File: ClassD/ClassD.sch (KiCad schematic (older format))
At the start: 28 parts, among them SW1 SW_PUSH, U1 TPA2008D2

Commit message: Updated the schematic with some part numbers and parametrics
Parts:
- removed SW1: SW_PUSH, symbol SW_PUSH
- added P? (x2): BNC, symbol BNC
- added SW?: SPST, symbol SPST
- C1, C10, C3, C4: ConradPN (none) -> Value; Fieldname (none) -> Value; Voltage (none) -> 10 V
- C2: ConradPN (none) -> Value; DigiKeyPN Value -> 1276-2865-1-ND; Fieldname (none) -> Value; Voltage (none) -> 16 V
- C5: value 120 pF -> 220 pF; ConradPN (none) -> Value; DigiKeyPN Value -> 1276-1059-1-ND; Fieldname (none) -> Value; Voltage (none) -> 50 V
- C6, C7, C8, C9: ConradPN (none) -> Value; Fieldname (none) -> Value; Voltage (none) -> 16 V
- C? (x2): value 4.7 μF -> 470 nF; ConradPN (none) -> Value; Fieldname (none) -> Value; Voltage (none) -> 50 V
- C? (x4): ConradPN (none) -> Value; Fieldname (none) -> Value; Voltage (none) -> 50 V
- RV1: ConradPN (none) -> Value; DigiKeyPN (none) -> 3362P-503TLF-ND; Fieldname (none) -> Value; Voltage (none) -> Value
- U1: ConradPN (none) -> Value; DigiKeyPN (none) -> 296-17158-1-ND; Fieldname (none) -> Value; Voltage (none) -> Value

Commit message: Updated the BOM specifications and added a regulator for VDD
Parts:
- added C12, C13: 1 μF, symbol C
- added P1: CONN_01X02, symbol CONN_01X02
- added U2: MCP1703T-5002E, symbol MCP1703T-5002E
- L1, L2, L3, L4: renamed from L?; ConradPN (none) -> Value; DigiKeyPN (none) -> 587-2618-1-ND; Fieldname (none) -> Value; Voltage (none) -> Value
- P2: renamed from P?; ConradPN (none) -> Value; DigiKeyPN (none) -> CP-1401-ND; Fieldname (none) -> Value; Voltage (none) -> Value
- P3: renamed from P?; ConradPN (none) -> Value; DigiKeyPN (none) -> CP-1402-ND; Fieldname (none) -> Value; Voltage (none) -> Value
- SP1: renamed from SP?; ConradPN (none) -> Value; DigiKeyPN (none) -> CP-1401-ND; Fieldname (none) -> Value; Voltage (none) -> Value
- SP2: renamed from SP?; ConradPN (none) -> Value; DigiKeyPN (none) -> CP-1402-ND; Fieldname (none) -> Value; Voltage (none) -> Value
- SW1: renamed from SW?; DigiKeyPN P8086SCT-ND -> FSM2JSMAA-SI-ND
- gave numbers to parts that had none: 6
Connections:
- net labels added: VIN
- wire segments 87 -> 97
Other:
- moved on the sheet: C1, C10, C11, C14, C15, C16, C17, C18, C19, C2, C3, C4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

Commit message: Updated the digikey part numbers etc.
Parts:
- removed C2: 10 μF, symbol C
- added C2: 10 μF, symbol CP
- L1, L2, L3, L4: DigiKeyPN 587-2618-1-ND -> 490-8418-1-ND
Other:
- note added: "For higher frequency transients, spikes, or digital hash on the line, \na good low equivalent-series-resistance (ESR) ceramic capacitor, \ntypically 0.1 μF, placed as close as possible to the device V DD \nterminal works best. For filtering lower-frequency noise signals, \na larger aluminum electrolytic capacitor of 10 μF or greater \nplaced near the audio power amplifier is recommended."
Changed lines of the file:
@@
 VDD
 $Comp
-L GND #PWR01
+L GND #PWR4
 U 1 1 56B5F2B5
 P 5850 5650
-F 0 "#PWR01" H 5850 5400 50  0001 C CNN
+F 0 "#PWR4" H 5850 5400 50  0001 C CNN
 F 1 "GND" H 5850 5500 50  0000 C CNN
 F 2 "" H 5850 5650 50  0000 C CNN
@@
 $EndComp
 $Comp
-L C C2
-U 1 1 56B60670
-P 2950 2700
-F 0 "C2" H 3000 2800 50  0000 L CNN
-F 1 "10 μF" H 2700 2600 50  0000 L CNN
-F 2 "" H 2988 2550 50  0000 C CNN
-F 3 "" H 2950 2700 50  0000 C CNN
-F 4 " 1276-2865-1-ND " H 2950 2700 60  0001 C CNN "DigiKeyPN"
-F 5 "16 V" H 2800 2500 60  0000 C CNN "Voltage"
-F 6 "Value" H 2950 2700 60  0001 C CNN "ConradPN"
-F 7 "Value" H 2950 2700 60  0001 C CNN "Fieldname"
-	1    2950 2700
-	1    0    0    -1
-$EndComp
-$Comp
-L GND #PWR02
+L GND #PWR3
 U 1 1 56B607D9
 P 2650 3200
-F 0 "#PWR02" H 2650 2950 50  0001 C CNN
+F 0 "#PWR3" H 2650 2950 50  0001 C CNN
 F 1 "GND" H 2650 3050 50  0000 C CNN
 F 2 "" H 2650 3200 50  0000 C CNN
@@
 $EndComp
 $Comp
-L GND #PWR03
+L GND #PWR5
 U 1 1 56B60A69
 P 6350 5550
-F 0 "#PWR03" H 6350 5300 50  0001 C CNN
+F 0 "#PWR5" H 6350 5300 50  0001 C CNN
 F 1 "GND" H 6350 5400 50  0000 C CNN
 F 2 "" H 6350 5550 50  0000 C CNN
@@
 ~SHUTDOWN
 $Comp
-L GND #PWR04
+L GND #PWR1
 U 1 1 56B6395C
 P 2000 6000
-F 0 "#PWR04" H 2000 5750 50  0001 C CNN
+F 0 "#PWR1" H 2000 5750 50  0001 C CNN
 F 1 "GND" H 2000 5850 50  0000 C CNN
 F 2 "" H 2000 6000 50  0000 C CNN
@@
 F 2 "" H 7000 1900 50  0000 C CNN
 F 3 "" H 7000 1900 50  0000 C CNN
-F 4 "587-2618-1-ND" H 7000 1900 60  0001 C CNN "DigiKeyPN"
+F 4 "490-8418-1-ND" H 7000 1900 60  0001 C CNN "DigiKeyPN"
 F 5 "Value" H 7000 1900 60  0001 C CNN "Voltage"
 F 6 "Value" H 7000 1900 60  0001 C CNN "ConradPN"
@@
 F 2 "" H 7000 2550 50  0000 C CNN
 F 3 "" H 7000 2550 50  0000 C CNN
-F 4 "587-2618-1-ND" H 7000 2550 60  0001 C CNN "DigiKeyPN"
+F 4 "490-8418-1-ND" H 7000 2550 60  0001 C CNN "DigiKeyPN"
 F 5 "Value" H 7000 2550 60  0001 C CNN "Voltage"
 F 6 "Value" H 7000 2550 60  0001 C CNN "ConradPN"
@@
 F 2 "" H 7150 3350 50  0000 C CNN
 F 3 "" H 7150 3350 50  0000 C CNN
-F 4 "587-2618-1-ND" H 7150 3350 60  0001 C CNN "DigiKeyPN"
+F 4 "490-8418-1-ND" H 7150 3350 60  0001 C CNN "DigiKeyPN"
 F 5 "Value" H 7150 3350 60  0001 C CNN "Voltage"
 F 6 "Value" H 7150 3350 60  0001 C CNN "ConradPN"
@@
 F 2 "" H 7150 4050 50  0000 C CNN
 F 3 "" H 7150 4050 50  0000 C CNN
-F 4 "587-2618-1-ND" H 7150 4050 60  0001 C CNN "DigiKeyPN"
+F 4 "490-8418-1-ND" H 7150 4050 60  0001 C CNN "DigiKeyPN"
 F 5 "Value" H 7150 4050 60  0001 C CNN "Voltage"
 F 6 "Value" H 7150 4050 60  0001 C CNN "ConradPN"
@@
 $EndComp
 $Comp
-L GND #PWR05
+L GND #PWR6
 U 1 1 56B66F4B
 P 7800 2300
-F 0 "#PWR05" H 7800 2050 50  0001 C CNN
+F 0 "#PWR6" H 7800 2050 50  0001 C CNN
 F 1 "GND" H 7800 2150 50  0000 C CNN
 F 2 "" H 7800 2300 50  0000 C CNN
@@
 $EndComp
 $Comp
-L GND #PWR06
+L GND #PWR8
 U 1 1 56B6779F
 P 8150 3800
-F 0 "#PWR06" H 8150 3550 50  0001 C CNN
+F 0 "#PWR8" H 8150 3550 50  0001 C CNN
 F 1 "GND" H 8150 3650 50  0000 C CNN
 F 2 "" H 8150 3800 50  0000 C CNN
@@
 $EndComp
 $Comp
-L GND #PWR07
+L GND #PWR9
 U 1 1 56B68F55
 P 8150 4550
-F 0 "#PWR07" H 8150 4300 50  0001 C CNN
+F 0 "#PWR9" H 8150 4300 50  0001 C CNN
 F 1 "GND" H 8150 4400 50  0000 C CNN
 F 2 "" H 8150 4550 50  0000 C CNN
@@
 $EndComp
 $Comp
-L GND #PWR08
+L GND #PWR7
 U 1 1 56B692A2
 P 7800 3000
-F 0 "#PWR08" H 7800 2750 50  0001 C CNN
+F 0 "#PWR7" H 7800 2750 50  0001 C CNN
 F 1 "GND" H 7800 2850 50  0000 C CNN
 F 2 "" H 7800 3000 50  0000 C CNN
@@
 	2450 1250 2450 1750
 $Comp
-L GND #PWR09
+L GND #PWR2
 U 1 1 56B7932F
 P 2450 1750
-F 0 "#PWR09" H 2450 1500 50  0001 C CNN
+F 0 "#PWR2" H 2450 1500 50  0001 C CNN
 F 1 "GND" H 2450 1600 50  0000 C CNN
 F 2 "" H 2450 1750 50  0000 C CNN
@@
 	7400 2250 7400 2550
 Connection ~ 7400 2550
+Text Notes 7900 5600 0    60   ~ 0
+For higher frequency transients, spikes, or digital hash on the line, \na good low equivalent-series-resistance (ESR) ceramic capacitor, \ntypically 0.1 μF, placed as close as possible to the device V DD \nterminal works best. For filtering lower-frequency noise signals, \na larger aluminum electrolytic capacitor of 10 μF or greater \nplaced near the audio power amplifier is recommended.
+$Comp
+L CP C2
+U 1 1 56B8FB66
+P 2950 2700
+F 0 "C2" H 2975 2800 50  0000 L CNN
+F 1 "10 μF" H 2700 2600 50  0000 L CNN
+F 2 "" H 2988 2550 50  0000 C CNN
+F 3 "" H 2950 2700 50  0000 C CNN
+F 4 "493-2181-1-ND" H 2950 2700 60  0001 C CNN "DigiKeyPN"
+F 5 "16 V" H 2800 2500 60  0000 C CNN "Voltage"
+F 6 "Value" H 2950 2700 60  0001 C CNN "ConradPN"
+F 7 "Value" H 2950 2700 60  0001 C CNN "Fieldname"
+	1    2950 2700
+	1    0    0    -1
+$EndComp
 $EndSCHEMATC

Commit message: Updated the speaker with the link to digi-key
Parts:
- SP1, SP2: Fieldname Value -> (none); Link (none) -> http://www.digikey.de/product-detail/de/AS07108PO-R/668-137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
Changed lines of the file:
@@
 F 5 "Value" H 9100 3700 60  0001 C CNN "Voltage"
 F 6 "Value" H 9100 3700 60  0001 C CNN "ConradPN"
-F 7 "Value" H 9100 3700 60  0001 C CNN "Fieldname"
+F 7 "http://www.digikey.de/product-detail/de/AS07108PO-R/668-1371-ND/1745572" H 9100 3700 60  0001 C CNN "Link"
 	1    9100 3700
 	1    0    0    -1
@@
 F 5 "Value" H 9100 2200 60  0001 C CNN "Voltage"
 F 6 "Value" H 9100 2200 60  0001 C CNN "ConradPN"
-F 7 "Value" H 9100 2200 60  0001 C CNN "Fieldname"
+F 7 "http://www.digikey.de/product-detail/de/AS07108PO-R/668-1371-ND/1745572" H 9100 2200 60  0001 C CNN "Link"
 	1    9100 2200
 	1    0    0    -1

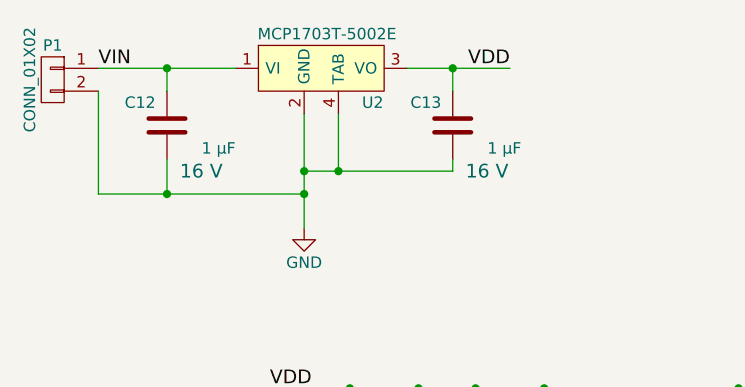
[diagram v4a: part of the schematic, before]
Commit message: Changed the voltage regulator to 1A (for the 4Ohm case)
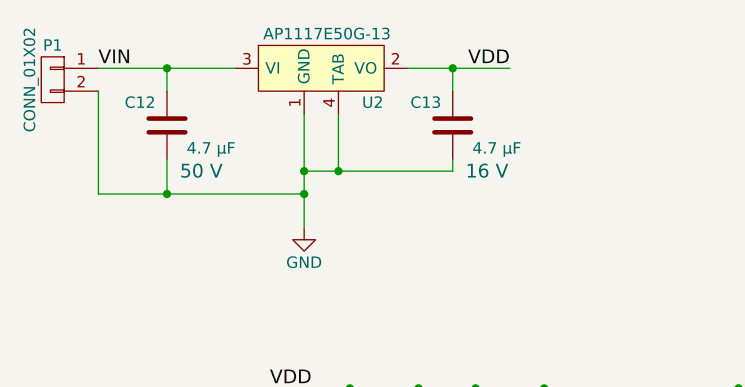
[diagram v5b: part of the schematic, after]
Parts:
- removed U2: MCP1703T-5002E, symbol MCP1703T-5002E
- added U2: AP1117E50G-13, symbol AP1117E50G-13
- C12: value 1 μF -> 4.7 μF; Voltage 16 V -> 50 V
- C13: value 1 μF -> 4.7 μF
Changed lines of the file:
@@
 Wire Wire Line
 	8700 3800 8800 3800
-$Comp
-L MCP1703T-5002E U2
-U 1 1 56B7910E
-P 2450 1050
-F 0 "U2" H 2750 900 50  0000 C CNN
-F 1 "MCP1703T-5002E" H 2550 1200 50  0000 C CNN
-F 2 "" H 2450 1050 50  0000 C CNN
-F 3 "" H 2450 1050 50  0000 C CNN
-F 4 "MCP1703T-5002E/DBCT-ND" H 2450 1050 60  0001 C CNN "DigiKeyPN"
-F 5 "Value" H 2450 1050 60  0001 C CNN "Voltage"
-F 6 "Value" H 2450 1050 60  0001 C CNN "ConradPN"
-F 7 "Value" H 2450 1050 60  0001 C CNN "Fieldname"
-	1    2450 1050
-	1    0    0    -1
-$EndComp
 Wire Wire Line
 	2600 1250 2600 1500
@@
 P 1850 1300
 F 0 "C12" H 1900 1200 50  0000 L CNN
-F 1 "1 μF" H 1550 1400 50  0000 L CNN
+F 1 "4.7 μF" H 1550 1400 50  0000 L CNN
 F 2 "" H 1888 1150 50  0000 C CNN
 F 3 "" H 1850 1300 50  0000 C CNN
 F 4 "Value" H 1850 1300 60  0001 C CNN "DigiKeyPN"
-F 5 "16 V" H 1700 1500 60  0000 C CNN "Voltage"
+F 5 "50 V" H 1700 1500 60  0000 C CNN "Voltage"
 F 6 "Value" H 1850 1300 60  0001 C CNN "ConradPN"
 F 7 "Value" H 1850 1300 60  0001 C CNN "Fieldname"
@@
 P 3100 1300
 F 0 "C13" H 3150 1200 50  0000 L CNN
-F 1 "1 μF" H 2800 1400 50  0000 L CNN
+F 1 "4.7 μF" H 2800 1400 50  0000 L CNN
 F 2 "" H 3138 1150 50  0000 C CNN
 F 3 "" H 3100 1300 50  0000 C CNN
@@
 	1    0    0    -1
 $EndComp
+$Comp
+L AP1117E50G-13 U2
+U 1 1 56BA2D73
+P 2450 1050
+F 0 "U2" H 2750 900 50  0000 C CNN
+F 1 "AP1117E50G-13" H 2550 1200 50  0000 C CNN
+F 2 "" H 2450 1050 50  0000 C CNN
+F 3 "" H 2450 1050 50  0000 C CNN
+F 4 "AP1117E50GDICT-ND" H 2450 1050 60  0001 C CNN "DigiKeyPN"
+F 5 "Value" H 2450 1050 60  0001 C CNN "Voltage"
+F 6 "Value" H 2450 1050 60  0001 C CNN "ConradPN"
+F 7 "http://www.digikey.de/product-detail/de/AP1117E50G-13/AP1117E50GDICT-ND/1301523" H 2450 1050 60  0001 C CNN "Link"
+	1    2450 1050
+	1    0    0    -1
+$EndComp

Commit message: Updated speaker specs
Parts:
- added R1: NOPOP, symbol R
- SP1: DigiKeyPN CP-1401-ND -> GF0771-ND; Link http://www.digikey.de/product-detail/de/AS07108PO-R/668-137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 -> http://www.digikey.de/product-detail/de/GF0771/GF0771-ND/30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
- SP2: DigiKeyPN CP-1402-ND -> GF0771-ND; Link http://www.digikey.de/product-detail/de/AS07108PO-R/668-137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 -> http://www.digikey.de/product-detail/de/GF0771/GF0771-ND/30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
- renumbered C12 to C1, C15 to C10, C18 to C11, C8 to C12, C6 to C13, C9 to C14, C7 to C15, C19 to C16, C5 to C17, C10 to C18, C11 to C19, C13 to C2, C14 to C3, C16 to C4, C1 to C5, C2 to C6, C3 to C7, C4 to C8, C17 to C9, R1 to R3, U2 to U1, U1 to U2
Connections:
- net labels removed: SHUTDOWN
- wire segments 97 -> 101
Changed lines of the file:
@@
 $EndDescr
 $Comp
-L C C8
+L C C12
 U 1 1 56B5D94C
 P 4700 3650
-F 0 "C8" V 4750 3700 50  0000 L CNN
+F 0 "C12" V 4750 3700 50  0000 L CNN
 F 1 "0.1 μF" V 4650 3350 50  0000 L CNN
 F 2 "" H 4738 3500 50  0000 C CNN
@@
 $EndComp
 $Comp
-L TPA2008D2 U1
+L TPA2008D2 U2
 U 1 1 56B5ECDC
 P 5550 4150
-F 0 "U1" H 5950 3050 60  0000 C CNN
+F 0 "U2" H 5950 3050 60  0000 C CNN
 F 1 "TPA2008D2" V 5500 4150 60  0000 C CNN
 F 2 "" H 5500 4300 60  0000 C CNN
@@
 $EndComp
 $Comp
-L C C6
+L C C13
 U 1 1 56B5EEF7
 P 4300 3850
-F 0 "C6" V 4350 3900 50  0000 L CNN
+F 0 "C13" V 4350 3900 50  0000 L CNN
 F 1 "0.1 μF" V 4250 3550 50  0000 L CNN
 F 2 "" H 4338 3700 50  0000 C CNN
@@
 $EndComp
 $Comp
-L C C9
+L C C14
 U 1 1 56B5EF1A
 P 4700 4050
-F 0 "C9" V 4750 4100 50  0000 L CNN
+F 0 "C14" V 4750 4100 50  0000 L CNN
 F 1 "0.1 μF" V 4650 3750 50  0000 L CNN
 F 2 "" H 4738 3900 50  0000 C CNN
@@
 $EndComp
 $Comp
-L C C7
+L C C15
 U 1 1 56B5EF3C
 P 4300 4250
-F 0 "C7" V 4350 4350 50  0000 L CNN
+F 0 "C15" V 4350 4350 50  0000 L CNN
 F 1 "0.1 μF" V 4250 3950 50  0000 L CNN
 F 2 "" H 4338 4100 50  0000 C CNN
@@
 VDD
 $Comp
-L GND #PWR4
+L GND #PWR8
 U 1 1 56B5F2B5
 P 5850 5650
-F 0 "#PWR4" H 5850 5400 50  0001 C CNN
+F 0 "#PWR8" H 5850 5400 50  0001 C CNN
 F 1 "GND" H 5850 5500 50  0000 C CNN
 F 2 "" H 5850 5650 50  0000 C CNN
@@
 $EndComp
 $Comp
-L R R1
+L R R3
 U 1 1 56B5F3A2
 P 4700 5150
-F 0 "R1" V 4780 5150 50  0000 C CNN
+F 0 "R3" V 4780 5150 50  0000 C CNN
 F 1 "120 kΩ" V 4600 5150 50  0000 C CNN
 F 2 "" V 4630 5150 50  0000 C CNN
@@
 $EndComp
 $Comp
-L C C5
+L C C17
 U 1 1 56B5F46C
 P 4250 5100
-F 0 "C5" H 4300 5200 50  0000 L CNN
+F 0 "C17" H 4300 5200 50  0000 L CNN
 F 1 "220 pF" H 3950 5000 50  0000 L CNN
 F 2 "" H 4288 4950 50  0000 C CNN
@@
 LOUT-
 $Comp
-L C C10
+L C C18
 U 1 1 56B5FCBA
 P 6350 5100
-F 0 "C10" H 6400 5000 50  0000 L CNN
+F 0 "C18" H 6400 5000 50  0000 L CNN
 F 1 "1 μF" H 6150 5200 50  0000 L CNN
 F 2 "" H 6388 4950 50  0000 C CNN
@@
 $EndComp
 $Comp
-L C C1
+L C C5
 U 1 1 56B600E8
 P 2650 2700
-F 0 "C1" H 2700 2800 50  0000 L CNN
+F 0 "C5" H 2700 2800 50  0000 L CNN
 F 1 "1 μF" H 2450 2600 50  0000 L CNN
 F 2 "" H 2688 2550 50  0000 C CNN
@@
 $EndComp
 $Comp
-L GND #PWR3
+L GND #PWR4
 U 1 1 56B607D9
 P 2650 3200
-F 0 "#PWR3" H 2650 2950 50  0001 C CNN
+F 0 "#PWR4" H 2650 2950 50  0001 C CNN
 F 1 "GND" H 2650 3050 50  0000 C CNN
 F 2 "" H 2650 3200 50  0000 C CNN
@@
 $EndComp
 $Comp
-L GND #PWR5
+L GND #PWR7
 U 1 1 56B60A69
 P 6350 5550
-F 0 "#PWR5" H 6350 5300 50  0001 C CNN
+F 0 "#PWR7" H 6350 5300 50  0001 C CNN
 F 1 "GND" H 6350 5400 50  0000 C CNN
 F 2 "" H 6350 5550 50  0000 C CNN
@@
 $EndComp
 $Comp
-L C C3
+L C C7
 U 1 1 56B60FFE
 P 3200 2700
-F 0 "C3" H 3250 2800 50  0000 L CNN
+F 0 "C7" H 3250 2800 50  0000 L CNN
 F 1 "1 μF" H 3000 2600 50  0000 L CNN
 F 2 "" H 3238 2550 50  0000 C CNN
@@
 $EndComp
 $Comp
-L C C4
+L C C8
 U 1 1 56B61005
 P 3500 2700
-F 0 "C4" H 3550 2800 50  0000 L CNN
+F 0 "C8" H 3550 2800 50  0000 L CNN
 F 1 "1 μF" H 3300 2600 50  0000 L CNN
 F 2 "" H 3538 2550 50  0000 C CNN
@@
 VDD1
 $Comp
-L C C11
+L C C19
 U 1 1 56B61EF5
 P 7350 5100
-F 0 "C11" H 7400 5000 50  0000 L CNN
+F 0 "C19" H 7400 5000 50  0000 L CNN
 F 1 "NO-POP" H 7150 5200 50  0000 L CNN
 F 2 "" H 7388 4950 50  0000 C CNN
@@
 ~SHUTDOWN
 $Comp
-L GND #PWR1
+L GND #PWR9
 U 1 1 56B6395C
 P 2000 6000
-F 0 "#PWR1" H 2000 5750 50  0001 C CNN
+F 0 "#PWR9" H 2000 5750 50  0001 C CNN
 F 1 "GND" H 2000 5850 50  0000 C CNN
 F 2 "" H 2000 6000 50  0000 C CNN
@@
 $EndComp
 Text Label 3650 3450 0    60   ~ 0
-SHUTDOWN
+~SHUTDOWN
 Text Notes 2700 7300 0    60   ~ 0
 A star point should be used for power, where the supply voltage for VDD, PVDD, \nand the volume circuitry can be taken. This point is typically at the bulk decoupling \ncapacitor. The trace connecting the star point to a potentiometer or a DAC should \nbe short. The trace connecting the potentiometer or DAC to the VOLUME pin \nshould be kept as short and straight as possible.\n\nAs with the VDD, a star ground should likewise be used. There should exist on the \nboard a point where AGND and PGND converge. This should be the only place \nwhere the two grounds are connected. The ground used for the volume control \nshould be AGND. If a potentiometer is to be used to control the volume of the \ndevice, it should be connected to AGND. A DAC that has a ground reference \nshould have a short trace to AGND from its ground reference input.\n
@@
 $EndComp
 $Comp
-L C C14
+L C C3
 U 1 1 56B66BA9
 P 7400 2100
-F 0 "C14" H 7450 2000 50  0000 L CNN
+F 0 "C3" H 7450 2000 50  0000 L CNN
 F 1 "470 nF" H 7100 2200 50  0000 L CNN
 F 2 "" H 7438 1950 50  0000 C CNN
@@
 $EndComp
 $Comp
-L C C16
+L C C4
 U 1 1 56B66DA2
 P 7800 2100
-F 0 "C16" H 7850 2000 50  0000 L CNN
+F 0 "C4" H 7850 2000 50  0000 L CNN
 F 1 "0.1 μF" H 7500 2200 50  0000 L CNN
 F 2 "" H 7838 1950 50  0000 C CNN
@@
 $EndComp
 $Comp
-L GND #PWR6
+L GND #PWR2
 U 1 1 56B66F4B
 P 7800 2300
-F 0 "#PWR6" H 7800 2050 50  0001 C CNN
+F 0 "#PWR2" H 7800 2050 50  0001 C CNN
 F 1 "GND" H 7800 2150 50  0000 C CNN
 F 2 "" H 7800 2300 50  0000 C CNN
@@
 $EndComp
 $Comp
-L C C15
+L C C10
 U 1 1 56B67792
 P 7750 3600
-F 0 "C15" H 7800 3500 50  0000 L CNN
+F 0 "C10" H 7800 3500 50  0000 L CNN
 F 1 "470 nF" H 7450 3700 50  0000 L CNN
 F 2 "" H 7788 3450 50  0000 C CNN
@@
 $EndComp
 $Comp
-L C C18
+L C C11
 U 1 1 56B67799
 P 8150 3600
-F 0 "C18" H 8200 3500 50  0000 L CNN
+F 0 "C11" H 8200 3500 50  0000 L CNN
 F 1 "0.1 μF" H 7850 3700 50  0000 L CNN
 F 2 "" H 8188 3450 50  0000 C CNN
@@
 $EndComp
 $Comp
-L GND #PWR8
+L GND #PWR5
 U 1 1 56B6779F
 P 8150 3800
-F 0 "#PWR8" H 8150 3550 50  0001 C CNN
+F 0 "#PWR5" H 8150 3550 50  0001 C CNN
 F 1 "GND" H 8150 3650 50  0000 C CNN
 F 2 "" H 8150 3800 50  0000 C CNN
@@
 $EndComp
 $Comp
-L C C19
+L C C16
 U 1 1 56B68EBB
 P 8150 4300
-F 0 "C19" H 8200 4200 50  0000 L CNN
+F 0 "C16" H 8200 4200 50  0000 L CNN
 F 1 "0.1 μF" H 7850 4400 50  0000 L CNN
 F 2 "" H 8188 4150 50  0000 C CNN
@@
 $EndComp
 $Comp
-L GND #PWR9
+L GND #PWR6
 U 1 1 56B68F55
 P 8150 4550
-F 0 "#PWR9" H 8150 4300 50  0001 C CNN
+F 0 "#PWR6" H 8150 4300 50  0001 C CNN
 F 1 "GND" H 8150 4400 50  0000 C CNN
 F 2 "" H 8150 4550 50  0000 C CNN
@@
 $EndComp
 $Comp
-L C C17
+L C C9
 U 1 1 56B69221
 P 7800 2750
-F 0 "C17" H 7850 2650 50  0000 L CNN
+F 0 "C9" H 7850 2650 50  0000 L CNN
 F 1 "0.1 μF" H 7500 2850 50  0000 L CNN
 F 2 "" H 7838 2600 50  0000 C CNN
@@
 $EndComp
 $Comp
-L GND #PWR7
+L GND #PWR3
 U 1 1 56B692A2
 P 7800 3000
-F 0 "#PWR7" H 7800 2750 50  0001 C CNN
+F 0 "#PWR3" H 7800 2750 50  0001 C CNN
 F 1 "GND" H 7800 2850 50  0000 C CNN
 F 2 "" H 7800 3000 50  0000 C CNN
@@
 F 2 "" H 9100 3700 50  0000 C CNN
 F 3 "" H 9100 3700 50  0000 C CNN
-F 4 "CP-1402-ND" H 9100 3700 60  0001 C CNN "DigiKeyPN"
+F 4 "GF0771-ND" H 9100 3700 60  0001 C CNN "DigiKeyPN"
 F 5 "Value" H 9100 3700 60  0001 C CNN "Voltage"
 F 6 "Value" H 9100 3700 60  0001 C CNN "ConradPN"
-F 7 "http://www.digikey.de/product-detail/de/AS07108PO-R/668-1371-ND/1745572" H 9100 3700 60  0001 C CNN "Link"
+F 7 "http://www.digikey.de/product-detail/de/GF0771/GF0771-ND/304442" H 9100 3700 60  0001 C CNN "Link"
 	1    9100 3700
 	1    0    0    -1
@@
 F 2 "" H 9100 2200 50  0000 C CNN
 F 3 "" H 9100 2200 50  0000 C CNN
-F 4 "CP-1401-ND" H 9100 2200 60  0001 C CNN "DigiKeyPN"
+F 4 "GF0771-ND" H 9100 2200 60  0001 C CNN "DigiKeyPN"
 F 5 "Value" H 9100 2200 60  0001 C CNN "Voltage"
 F 6 "Value" H 9100 2200 60  0001 C CNN "ConradPN"
-F 7 "http://www.digikey.de/product-detail/de/AS07108PO-R/668-1371-ND/1745572" H 9100 2200 60  0001 C CNN "Link"
+F 7 "http://www.digikey.de/product-detail/de/GF0771/GF0771-ND/304442" H 9100 2200 60  0001 C CNN "Link"
 	1    9100 2200
 	1    0    0    -1
@@
 	2450 1250 2450 1750
 $Comp
-L GND #PWR2
+L GND #PWR1
 U 1 1 56B7932F
 P 2450 1750
-F 0 "#PWR2" H 2450 1500 50  0001 C CNN
+F 0 "#PWR1" H 2450 1500 50  0001 C CNN
 F 1 "GND" H 2450 1600 50  0000 C CNN
 F 2 "" H 2450 1750 50  0000 C CNN
@@
 	2900 1050 3350 1050
 $Comp
-L C C12
+L C C1
 U 1 1 56B7956C
 P 1850 1300
-F 0 "C12" H 1900 1200 50  0000 L CNN
+F 0 "C1" H 1900 1200 50  0000 L CNN
 F 1 "4.7 μF" H 1550 1400 50  0000 L CNN
 F 2 "" H 1888 1150 50  0000 C CNN
@@
 $EndComp
 $Comp
-L C C13
+L C C2
 U 1 1 56B79688
 P 3100 1300
-F 0 "C13" H 3150 1200 50  0000 L CNN
+F 0 "C2" H 3150 1200 50  0000 L CNN
 F 1 "4.7 μF" H 2800 1400 50  0000 L CNN
 F 2 "" H 3138 1150 50  0000 C CNN
@@
 For higher frequency transients, spikes, or digital hash on the line, \na good low equivalent-series-resistance (ESR) ceramic capacitor, \ntypically 0.1 μF, placed as close as possible to the device V DD \nterminal works best. For filtering lower-frequency noise signals, \na larger aluminum electrolytic capacitor of 10 μF or greater \nplaced near the audio power amplifier is recommended.
 $Comp
-L CP C2
+L CP C6
 U 1 1 56B8FB66
 P 2950 2700
-F 0 "C2" H 2975 2800 50  0000 L CNN
+F 0 "C6" H 2975 2800 50  0000 L CNN
 F 1 "10 μF" H 2700 2600 50  0000 L CNN
 F 2 "" H 2988 2550 50  0000 C CNN
@@
 $EndComp
 $Comp
-L AP1117E50G-13 U2
+L AP1117E50G-13 U1
 U 1 1 56BA2D73
 P 2450 1050
-F 0 "U2" H 2750 900 50  0000 C CNN
+F 0 "U1" H 2750 900 50  0000 C CNN
 F 1 "AP1117E50G-13" H 2550 1200 50  0000 C CNN
 F 2 "" H 2450 1050 50  0000 C CNN
@@
 	1    0    0    -1
 $EndComp
+$Comp
+L R R1
+U 1 1 56BB8A9C
+P 2550 700
+F 0 "R1" V 2630 700 50  0000 C CNN
+F 1 "NOPOP" V 2550 700 50  0000 C CNN
+F 2 "" V 2480 700 50  0000 C CNN
+F 3 "" H 2550 700 50  0000 C CNN
+	1    2550 700
+	0    1    1    0
+$EndComp
+Wire Wire Line
+	2400 700  2000 700
+Wire Wire Line
+	2000 700  2000 1050
+Connection ~ 2000 1050
+Wire Wire Line
+	2700 700  3000 700
+Wire Wire Line
+	3000 700  3000 1050
+Connection ~ 3000 1050
 $EndSCHEMATC

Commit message: Started associating footprints to symbols and checking own stock
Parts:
- C1, C2, C5, C7, C8: footprint (none) -> Capacitors_SMD:C_1206; Link (none) -> Value; On-Hand (none) -> Yes
- C10, C11, C12, C13, C14, C15, C16, C17, C18, C3, C4: footprint (none) -> Capacitors_SMD:C_0805; Link (none) -> Value; On-Hand (none) -> Yes
- C19, C9: footprint (none) -> Capacitors_SMD:C_0805
- C6, L1, L2, L3, L4, SW1: Link (none) -> Value; On-Hand (none) -> Yes
- P1, R2, R3: ConradPN (none) -> Value; DigiKeyPN (none) -> Value; Link (none) -> Value; On-Hand (none) -> Yes; Voltage (none) -> Value
